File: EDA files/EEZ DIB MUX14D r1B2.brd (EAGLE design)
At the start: 131 x 95 mm, 56 parts, among them IC1 M24C32-WMN6P, IC2 74HC1G126GW,125, IC3 LP2985-33DBVR, IC4 STM32F030C6T6, IC5 ULN2803ADWR, IC6 ULN2803ADWR, K1 3572.1220.051, K10 3572.1220.051, K11 3572.1220.051, K12 3572.1220.051, K13 3572.1220.051, K14 3572.1220.051, K15 3572.1220.051, K16 3572.1220.051, K17 3572.1220.051, K2 3572.1220.051, K3 3572.1220.051, K4 3572.1220.051, K5 3572.1220.051, K6 3572.1220.051, K7 3572.1220.051, K8 3572.1220.051, K9 3572.1220.051, Q1 2N7002, X1 DS1014-10RF1B, X2 77317-104-28LF, X3 DS1014-10RF1B, X4 N.C., X5 691327310016, X6 691327310016

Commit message: K9, K8, K17 rotated on PCB
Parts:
- moved D1 11.2 mm to (50.2, 82.6), turned to 180 degrees
- moved ZD3 11.2 mm to (54.5, 82.6), turned to 0 degrees
- turned K17 to 180 degrees
- turned K8 to 180 degrees
- turned K9 to 180 degrees
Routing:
- net P1H: track 202.7 -> 240.6 mm
- net P1L: track 212.4 -> 238.0 mm, vias 1 -> 2
- net P1H_OUT: track 32.3 -> 8.69 mm
- net P2H_OUT: track 31.2 -> 8.13 mm
- net P2H: track 192.1 -> 209.6 mm, vias 2 -> 4
- net +5V: track 527.1 -> 543.9 mm, vias 15 -> 17
- net N$43: track 53.0 -> 66.6 mm
- net N$42: track 84.5 -> 97.3 mm
- net N$60: track 63.3 -> 75.5 mm
- net P1L_OUT: track 21.9 -> 14.3 mm
- net P2L_OUT: track 20.7 -> 13.7 mm
- net P2L: track 202.3 -> 203.1 mm, vias 1 -> 2

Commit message: ADIB ID=002
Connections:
- new net N$1: X1.10, X1.9
- new net N$2: X3.10, X3.9
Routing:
- net N$2: track 0.00 -> 2.00 mm
- net N$1: track 0.00 -> 2.00 mm
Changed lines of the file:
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@@
 <layer number="20" name="Dimension" color="12" fill="1" visible="yes" active="yes"/>
 <layer number="21" name="tPlace" color="7" fill="1" visible="yes" active="yes"/>
-<layer number="22" name="bPlace" color="6" fill="1" visible="no" active="yes"/>
+<layer number="22" name="bPlace" color="6" fill="1" visible="yes" active="yes"/>
 <layer number="23" name="tOrigins" color="15" fill="1" visible="yes" active="yes"/>
 <layer number="24" name="bOrigins" color="15" fill="1" visible="no" active="yes"/>
@@
 <layer number="56" name="wert" color="7" fill="1" visible="no" active="no"/>
 <layer number="57" name="tCAD" color="7" fill="1" visible="no" active="no"/>
+<layer number="88" name="SimResults" color="9" fill="1" visible="yes" active="yes"/>
+<layer number="89" name="SimProbes" color="9" fill="1" visible="yes" active="yes"/>
 <layer number="90" name="Modules" color="7" fill="1" visible="no" active="no"/>
 <layer number="91" name="Nets" color="2" fill="1" visible="no" active="no"/>
@@
 <layer number="113" name="bTPoint" color="7" fill="1" visible="no" active="no"/>
 <layer number="114" name="Änderung" color="7" fill="1" visible="no" active="no"/>
+<layer number="115" name="CH1" color="13" fill="1" visible="yes" active="yes"/>
 <layer number="116" name="Patch_BOT" color="7" fill="1" visible="no" active="no"/>
+<layer number="117" name="CH2" color="9" fill="1" visible="yes" active="yes"/>
 <layer number="118" name="Rect_Pads" color="7" fill="1" visible="no" active="no"/>
+<layer number="119" name="CH3" color="12" fill="1" visible="yes" active="yes"/>
 <layer number="120" name="lotbs" color="7" fill="1" visible="no" active="no"/>
 <layer number="121" name="_tsilk" color="7" fill="1" visible="no" active="no"/>
@@
 <layer number="127" name="_tValues" color="7" fill="1" visible="no" active="no"/>
 <layer number="128" name="_bValues" color="7" fill="1" visible="no" active="no"/>
+<layer number="129" name="sram_cmd" color="13" fill="1" visible="yes" active="yes"/>
+<layer number="130" name="sram_ctrl" color="2" fill="1" visible="yes" active="yes"/>
 <layer number="131" name="tAdjust" color="7" fill="1" visible="no" active="no"/>
 <layer number="132" name="bAdjust" color="7" fill="1" visible="no" active="no"/>
@@
 <wire x1="53.183" y1="82.6135" x2="51.5285" y2="82.6135" width="0.4064" layer="1"/>
 </signal>
+<signal name="N$1">
+<contactref element="X1" pad="9"/>
+<contactref element="X1" pad="10"/>
+<wire x1="49" y1="88" x2="49" y2="86" width="0.2032" layer="16"/>
+</signal>
+<signal name="N$2">
+<contactref element="X3" pad="9"/>
+<contactref element="X3" pad="10"/>
+<wire x1="69" y1="88" x2="69" y2="86" width="0.2032" layer="16"/>
+</signal>
 </signals>

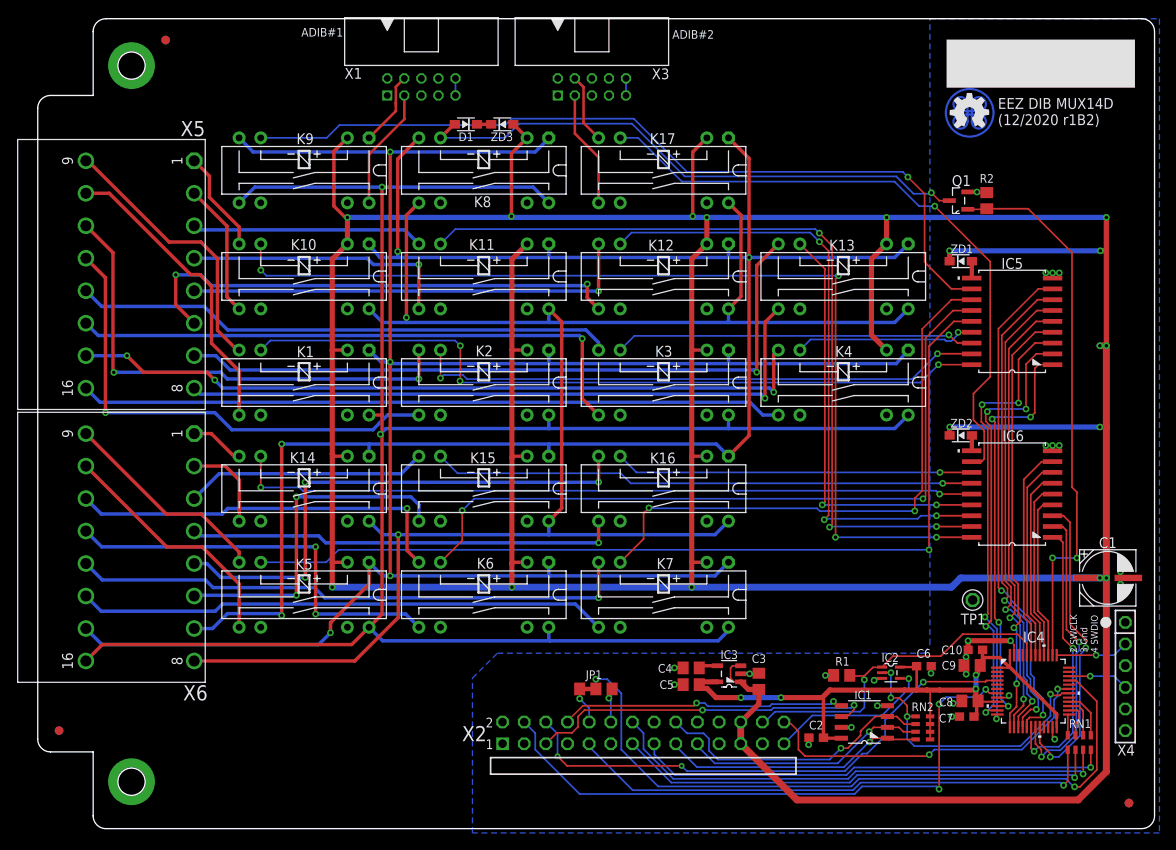
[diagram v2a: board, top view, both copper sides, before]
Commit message: small PCB layout corrections
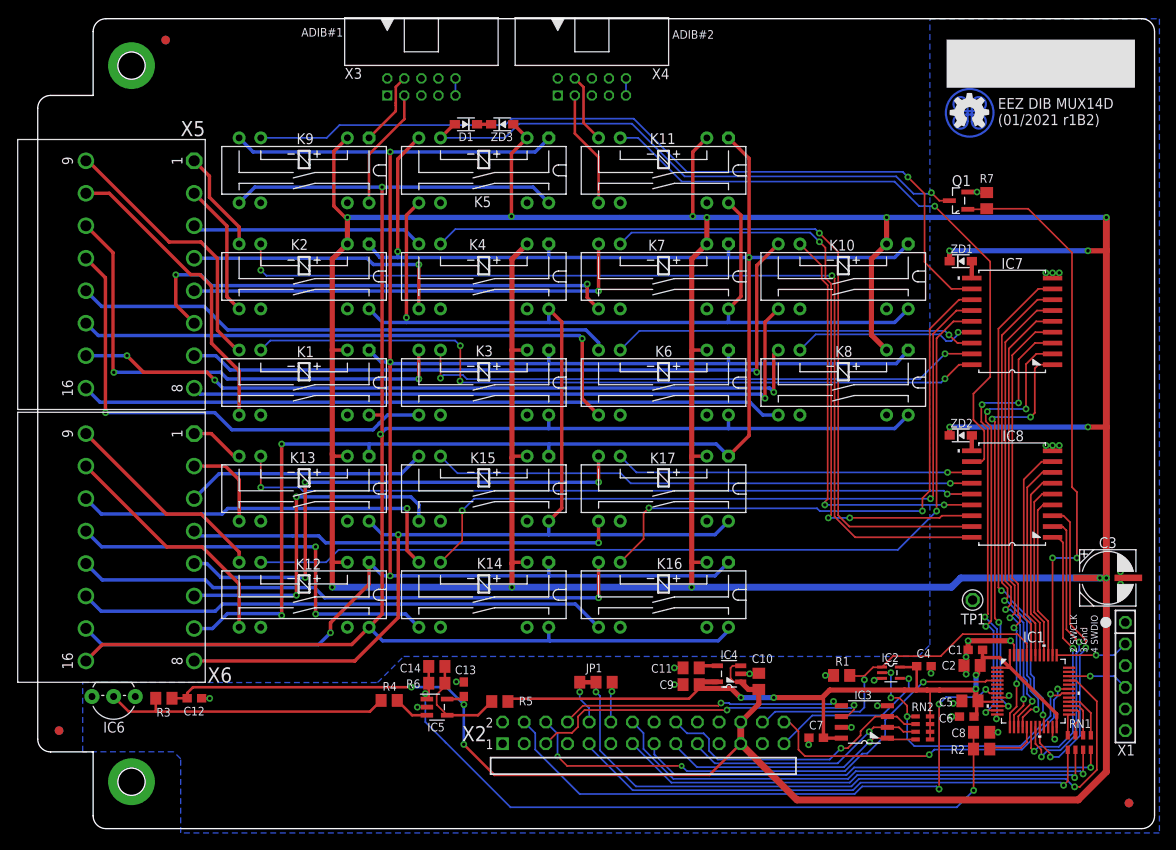
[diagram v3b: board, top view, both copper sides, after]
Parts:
- added C11: 10n, rcl:C0805
- added C12, C13: 100n, rcl:C0603
- added C14: 100p, rcl:C0805
- added IC7, IC8: ULN2803ADWR, EEZ_TI:DW18_TEX-M
- added R3: 1K5, rcl:R0805
- added R4, R5: 30K, rcl:R0805
- added R6: 120K, rcl:R0805
- added R7: 100K, rcl:R0805
- C1: value EEEFK1V470P -> 100n; device EEZ_Lib1:CAPAE660X610N -> rcl:C0603
- C10, C2: value 100n -> 2u2; device rcl:C0603 -> rcl:C0805
- C3: value 2u2 -> EEEFK1V470P; device rcl:C0805 -> EEZ_Lib1:CAPAE660X610N
- C4: value 10n -> 100n; device rcl:C0805 -> rcl:C0603
- C8: value 2u2 -> ???
- IC1: value M24C32-WMN6P -> STM32F030C6T6; device EEZ_Lib1:SOIC127P600X173-8N -> EEZ_DIB:LQFP-48
- IC3: value LP2985-33DBVR -> M24C32-WMN6P; device EEZ_DIB:SOT95P270X145-5N -> EEZ_Lib1:SOIC127P600X173-8N
- IC4: value STM32F030C6T6 -> LP2985-33DBVR; device EEZ_DIB:LQFP-48 -> EEZ_DIB:SOT95P270X145-5N
- IC5: value ULN2803ADWR -> TLV9001IDBVR; device EEZ_TI:DW18_TEX-M -> EEZ_TI:DBV5
- IC6: value ULN2803ADWR -> LM335; device EEZ_TI:DW18_TEX-M -> EEZ_TI:TO92
- R2: value 100K -> ???
- X1: value DS1014-10RF1B -> N.C.; device EEZ_connectors:DS1014-10RF1B -> con-samtec:SSW-106-02-S-S
- X4: value N.C. -> DS1014-10RF1B; device con-samtec:SSW-106-02-S-S -> EEZ_connectors:DS1014-10RF1B
- moved IC6 108.0 mm to (8.90, 15.5)
- moved X1 107.7 mm to (127.6, 17.8), turned to 270 degrees
- moved X4 93.3 mm to (65.0, 87.0), turned to 0 degrees
- moved IC5 81.2 mm to (46.8, 14.2), turned to 0 degrees
- moved K13 68.0 mm to (31.2, 39.9)
- moved R2 64.3 mm to (110.7, 9.33), turned to 180 degrees
- moved K10 63.2 mm to (94.5, 64.8)
- moved K12 56.3 mm to (31.2, 27.4)
- moved K5 54.1 mm to (52.3, 77.2)
- moved K8 49.0 mm to (94.5, 52.3)
- moved K4 44.0 mm to (52.3, 64.8)
- moved C3 42.7 mm to (125.5, 29.4), turned to 0 degrees
- moved K17 37.3 mm to (73.4, 39.9)
- moved K7 37.3 mm to (73.4, 64.8)
- moved IC4 35.7 mm to (81.1, 18.2), turned to 180 degrees
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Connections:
- removed net N$1 (its old number): X1.10, X1.9
- new net CJ_AIN: C14.2, C8.2, IC5.1, R2.2, R6.1
- new net N$183: C14.1, IC5.4, R5.1, R6.2
- new net N$184: IC5.3, R4.1
- new net N$2: X4.10, X4.9
- new net N$3: IC6.2, R3.2, R4.2
- new net N$6: IC1.17, R2.1
- net +3V3: now also C1.2, C2.1, C4.1, C5.2, C7.2, IC1.1, IC1.24, IC1.48, IC1.9, IC3.8, IC4.5, R5.2; no longer C10.2, C2.2, C5.1, C7.1, C8.2, IC1.8, IC3.5, IC4.1, IC4.24, IC4.48, IC4.9
- net +5V: now also C10.2, C12.1, C13.1, C3.1, IC4.1, IC4.3, IC5.5, R3.1; no longer C1.1, C3.2, IC3.1, IC3.3
- net BOOT0: now also IC1.44; no longer IC4.44
- net DIB_A0: now also IC3.1; no longer IC1.1
- net DIB_A1: now also IC3.2; no longer IC1.2
- net DIB_A2: now also IC3.3; no longer IC1.3
- net DIB_CSA: now also IC1.25; no longer IC4.25
- net DIB_MISO: now also IC1.27; no longer IC4.27
- net DIB_MOSI: now also IC1.28; no longer IC4.28
- net DIB_NRESET: now also IC1.7; no longer IC4.7
- net DIB_SCL: now also IC3.6; no longer IC1.6
- net DIB_SCLK: now also IC1.26; no longer IC4.26
- net DIB_SDA: now also IC3.5; no longer IC1.5
- net DIB_SYNC: now also IC1.4; no longer IC4.4
- net GND: now also C1.1, C11.1, C12.2, C13.2, C2.2, C3.2, C4.2, C5.1, C7.1, IC1.23, IC1.47, IC1.8, IC3.4, IC3.7, IC4.2, IC5.2, IC6.3, IC7.9, IC8.9, R7.2, X1.3; no longer C1.2, C2.1, C3.1, C4.1, C5.2, C7.2, IC1.4, IC1.7, IC3.2, IC4.23, IC4.47, IC4.8, IC5.9, IC6.9, R2.2, X4.3
- net N$28: now also IC7.10; no longer IC5.10
- net N$30: now also IC7.18; no longer IC5.18
- net N$32: now also IC7.17, K3.6; no longer IC5.17, K2.6
- net N$34: now also IC7.16, K6.6; no longer IC5.16, K3.6
- net N$35: now also IC7.15, K8.6; no longer IC5.15, K4.6
- net N$36: now also IC7.14, K12.6; no longer IC5.14, K5.6
- net N$38: now also IC7.13, K14.6; no longer IC5.13, K6.6
- net N$40: now also IC7.12, K16.6; no longer IC5.12, K7.6
- net N$42: now also IC7.11; no longer IC5.11
- net N$43: now also K5.6; no longer K8.6
- net N$44: now also IC8.10; no longer IC6.10
- net N$46: now also IC8.18, K2.6; no longer IC6.18, K10.6
- net N$48: now also IC8.17, K4.6; no longer IC6.17, K11.6
- net N$50: now also IC8.16, K7.6; no longer IC6.16, K12.6
- net N$52: now also IC8.15, K10.6; no longer IC6.15, K13.6
- net N$54: now also IC8.14, K13.6; no longer IC6.14, K14.6
- net N$56: now also IC8.13; no longer IC6.13
- net N$58: now also IC8.12, K17.6; no longer IC6.12, K16.6
- net N$60: now also IC8.11, K11.6; no longer IC6.11, K17.6
- net N$70: now also C11.2, IC4.4; no longer C4.2, IC3.4
- net N$75: now also IC1.33; no longer IC4.33
- net P1: now also IC1.21, IC7.8; no longer IC4.17, IC5.8
- net P1H: now also K12.1, K14.1, K16.1; no longer K2.1, K4.1, K7.1
- net P1H.2: now also K3.7; no longer K2.7
- net P1H.3: now also K6.7; no longer K3.7
- net P1H.4: now also K8.7; no longer K4.7
- net P1H.5: now also K12.7; no longer K5.7
- net P1H.6: now also K14.7; no longer K6.7
- net P1H.7: now also K16.7; no longer K7.7
- net P1H_OUT: now also X3.4; no longer X1.4
- net P1L: now also K12.14, K14.14, K16.14; no longer K2.14, K4.14, K7.14
- net P1L.2: now also K3.8; no longer K2.8
- net P1L.3: now also K6.8; no longer K3.8
- net P1L.4: now also K8.8; no longer K4.8
- net P1L.5: now also K12.8; no longer K5.8
- net P1L.6: now also K14.8; no longer K6.8
- net P1L.7: now also K16.8; no longer K7.8
- net P1L_OUT: now also X3.3; no longer X1.3
- net P2: now also IC1.43, IC8.8; no longer IC4.43, IC6.8
- net P2H: now also K2.1, K4.1, K5.7, K7.1; no longer K12.1, K14.1, K16.1, K8.7
- net P2H.1: now also K2.7; no longer K10.7
- net P2H.2: now also K4.7; no longer K11.7
- net P2H.3: now also K7.7; no longer K12.7
- net P2H.4: now also K10.7; no longer K13.7
- net P2H.5: now also K13.7; no longer K14.7
- net P2H.7: now also K17.7; no longer K16.7
- net P2H_OUT: now also K11.7, X4.4; no longer K17.7, X3.4
- net P2L: now also K2.14, K4.14, K5.8, K7.14; no longer K12.14, K14.14, K16.14, K8.8
- net P2L.1: now also K2.8; no longer K10.8
- net P2L.2: now also K4.8; no longer K11.8
- net P2L.3: now also K7.8; no longer K12.8
- net P2L.4: now also K10.8; no longer K13.8
- net P2L.5: now also K13.8; no longer K14.8
- net P2L.6: now also K17.8; no longer K16.8
- net P2L_OUT: now also K11.8, X4.3; no longer K17.8, X3.3
- net P2_EXT: now also IC1.38, R7.1; no longer IC4.38, R2.1
- net PORT_A0: now also IC1.10, IC7.1; no longer IC4.10, IC5.1
- net PORT_A1: now also IC1.11, IC7.2; no longer IC4.11, IC5.2
- net PORT_A2: now also IC1.12, IC7.3; no longer IC4.12, IC5.3
- net PORT_A3: now also IC1.13, IC7.4; no longer IC4.13, IC5.4
- net PORT_A4: now also IC1.14, IC7.5; no longer IC4.14, IC5.5
- net PORT_A5: now also IC1.15, IC7.6; no longer IC4.15, IC5.6
- net PORT_A6: now also IC1.16, IC7.7; no longer IC4.16, IC5.7
- net PORT_B0: now also IC1.18, IC8.1; no longer IC4.18, IC6.1
- net PORT_B1: now also IC1.19, IC8.2; no longer IC4.19, IC6.2
- net PORT_B2: now also IC1.20, IC8.3; no longer IC4.20, IC6.3
- net PORT_B3: now also IC1.39, IC8.4; no longer IC4.39, IC6.4
- net PORT_B4: now also IC1.40, IC8.5; no longer IC4.40, IC6.5
- net PORT_B5: now also IC1.41, IC8.6; no longer IC4.41, IC6.6
- net PORT_B6: now also IC1.42, IC8.7; no longer IC4.42, IC6.7
- net SWCLK: now also IC1.37, X1.2; no longer IC4.37, X4.2
- net SWDIO: now also IC1.34, X1.4; no longer IC4.34, X4.4
- net UART_RX: now also IC1.31; no longer IC4.31
- net UART_TX: now also IC1.30; no longer IC4.30
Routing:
- net CJ_AIN: track 0.00 -> 83.9 mm, vias 0 -> 2
- net +5V: track 543.9 -> 622.3 mm, vias 17 -> 18
- net N$3: track 0.00 -> 34.4 mm
- net +3V3: track 81.5 -> 105.2 mm
- net N$183: track 0.00 -> 12.5 mm
- net N$6: track 0.00 -> 6.45 mm
- net GND: track 29.4 -> 33.7 mm, vias 26 -> 30
- net N$184: track 0.00 -> 4.19 mm
- net N$36: track 109.1 -> 107.0 mm
- net N$46: track 117.9 -> 115.8 mm, vias 4 -> 2
- net N$2: track 0.00 -> 2.00 mm
- net N$1 (its old number): track 2.00 -> 0.00 mm
- net N$48: track 97.3 -> 95.6 mm, vias 3 -> 1
- net P1: track 58.9 -> 57.4 mm
- net DIB_IRQ: track 4.35 -> 5.13 mm
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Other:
- board text added: "EEZ DIB MUX14D (01/2021 r1B2)"
- board text added: "EEZ DIB MUX14D (01/2021 r1B2) Project source code: github.com/eez-open"
- board text removed: "EEZ DIB MUX14D (12/2020 r1B2)"
- board text removed: "EEZ DIB MUX14D (12/2020 r1B2) Project source code: github.com/eez-open"

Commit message: PCB ID added
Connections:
- new net N$7: IC1.5
- net GND: now also IC1.6
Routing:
- net GND: track 33.7 -> 35.7 mm
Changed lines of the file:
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@@
 <layer number="19" name="Unrouted" color="6" fill="1" visible="yes" active="yes"/>
 <layer number="20" name="Dimension" color="12" fill="1" visible="yes" active="yes"/>
-<layer number="21" name="tPlace" color="7" fill="1" visible="no" active="yes"/>
+<layer number="21" name="tPlace" color="7" fill="1" visible="yes" active="yes"/>
 <layer number="22" name="bPlace" color="6" fill="1" visible="no" active="yes"/>
 <layer number="23" name="tOrigins" color="15" fill="1" visible="yes" active="yes"/>
 <layer number="24" name="bOrigins" color="15" fill="1" visible="no" active="yes"/>
-<layer number="25" name="tNames" color="7" fill="1" visible="no" active="yes"/>
+<layer number="25" name="tNames" color="7" fill="1" visible="yes" active="yes"/>
 <layer number="26" name="bNames" color="5" fill="1" visible="no" active="yes"/>
 <layer number="27" name="tValues" color="10" fill="1" visible="no" active="yes"/>
@@
 <layer number="56" name="wert" color="7" fill="1" visible="no" active="no"/>
 <layer number="57" name="tCAD" color="7" fill="1" visible="no" active="no"/>
+<layer number="88" name="SimResults" color="9" fill="1" visible="yes" active="yes"/>
+<layer number="89" name="SimProbes" color="9" fill="1" visible="yes" active="yes"/>
 <layer number="90" name="Modules" color="7" fill="1" visible="no" active="no"/>
 <layer number="91" name="Nets" color="2" fill="1" visible="no" active="no"/>
@@
 <layer number="113" name="bTPoint" color="7" fill="1" visible="no" active="no"/>
 <layer number="114" name="Änderung" color="7" fill="1" visible="no" active="no"/>
+<layer number="115" name="CH1" color="13" fill="1" visible="yes" active="yes"/>
 <layer number="116" name="Patch_BOT" color="7" fill="1" visible="no" active="no"/>
+<layer number="117" name="CH2" color="9" fill="1" visible="yes" active="yes"/>
 <layer number="118" name="Rect_Pads" color="7" fill="1" visible="no" active="no"/>
+<layer number="119" name="CH3" color="12" fill="1" visible="yes" active="yes"/>
 <layer number="120" name="lotbs" color="7" fill="1" visible="no" active="no"/>
 <layer number="121" name="_tsilk" color="7" fill="1" visible="no" active="no"/>
@@
 <layer number="127" name="_tValues" color="7" fill="1" visible="no" active="no"/>
 <layer number="128" name="_bValues" color="7" fill="1" visible="no" active="no"/>
+<layer number="129" name="sram_cmd" color="13" fill="1" visible="yes" active="yes"/>
+<layer number="130" name="sram_ctrl" color="2" fill="1" visible="yes" active="yes"/>
 <layer number="131" name="tAdjust" color="7" fill="1" visible="no" active="no"/>
 <layer number="132" name="bAdjust" color="7" fill="1" visible="no" active="no"/>
@@
 <wire x1="49.9745" y1="17.1949" x2="49.1245" y2="17.1949" width="0.2032" layer="1"/>
 <wire x1="49.1245" y1="17.1949" x2="49.0982" y2="17.2212" width="0.2032" layer="1"/>
+<contactref element="IC1" pad="6"/>
+<wire x1="112.5601" y1="16.383" x2="113.7158" y2="16.383" width="0.2032" layer="1"/>
+<wire x1="113.7158" y1="16.383" x2="113.9317" y2="16.1671" width="0.2032" layer="1"/>
+<wire x1="113.9317" y1="16.1671" x2="113.9317" y2="15.6083" width="0.2032" layer="1"/>
 </signal>
 <signal name="DIB_A0">
@@
 <wire x1="60.9727" y1="8.4836" x2="60.9727" y2="11.1273" width="0.2032" layer="16"/>
 <wire x1="60.9727" y1="11.1273" x2="59.6" y2="12.5" width="0.2032" layer="16"/>
-<wire x1="103.8479" y1="17.1831" x2="99.4029" y2="12.7381" width="0.2032" layer="16"/>
-<wire x1="99.4029" y1="12.7381" x2="99.4029" y2="10.922" width="0.2032" layer="16"/>
 <wire x1="99.4029" y1="10.922" x2="97.282" y2="8.8011" width="0.2032" layer="16"/>
 <wire x1="97.282" y1="8.8011" x2="96.7359" y2="8.8011" width="0.2032" layer="16"/>
@@
 <wire x1="103.9241" y1="17.2339" x2="103.8733" y2="17.1831" width="0.2032" layer="1"/>
 <wire x1="103.8733" y1="17.1831" x2="103.8479" y2="17.1831" width="0.2032" layer="16"/>
+<wire x1="99.4029" y1="10.922" x2="99.4029" y2="12.3571" width="0.2032" layer="16"/>
+<wire x1="99.4029" y1="12.3571" x2="103.8479" y2="16.8021" width="0.2032" layer="16"/>
+<wire x1="103.8479" y1="17.1831" x2="103.8479" y2="16.8021" width="0.2032" layer="16"/>
 </signal>
 <signal name="P2H_OUT">
@@
 <wire x1="43.9116" y1="13.2994" x2="42.1742" y2="15.0368" width="0.3048" layer="1"/>
 </signal>
+<signal name="N$7">
+<contactref element="IC1" pad="5"/>
+</signal>
 </signals>
